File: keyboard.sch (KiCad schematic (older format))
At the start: 14 parts, among them CN5 Conn_01x25, U16 74LS14, U27 LM556, U29 7406, U37 7406

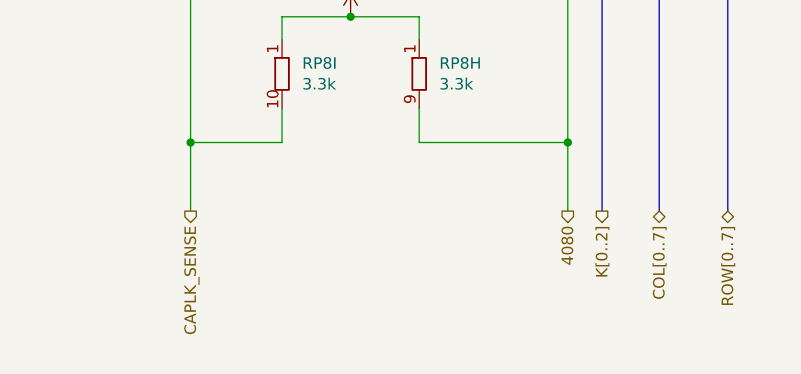
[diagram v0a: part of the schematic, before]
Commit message: Clean up schematic
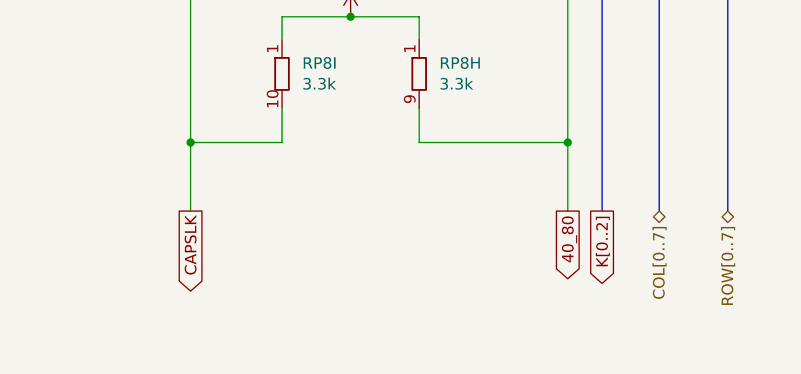
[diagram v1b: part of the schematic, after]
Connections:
- net 4080 renamed 40_80
- net CAPLK_SENSE renamed CAPSLK
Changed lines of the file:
@@
 Wire Wire Line
 	2750 5050 3150 5050
-Text HLabel 3300 6500 3    50   Output ~ 0
-K[0..2]
-Text HLabel 3150 6500 3    50   Output ~ 0
-4080
 Wire Wire Line
 	3150 5050 3150 6200
@@
 	1    0    0    -1
 $EndComp
-Text HLabel 1500 6500 3    50   Output ~ 0
-CAPLK_SENSE
 Wire Wire Line
 	1900 6050 1900 6200
@@
 Wire Bus Line
 	3550 3950 3550 6500
+Text GLabel 1500 6500 3    50   Output ~ 0
+CAPSLK
+Text GLabel 3150 6500 3    50   Output ~ 0
+40_80
+Text GLabel 3300 6500 3    50   Output ~ 0
+K[0..2]
 $EndSCHEMATC
